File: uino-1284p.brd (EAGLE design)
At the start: 68.6 x 53.3 mm, 59 parts, among them J1 Micro USB, J2 M03X2, J3 CON_TERMINAL_BLOCK_02-5MM, J4 M03X2, J5 IO, U1 ATMEGA8U2AU, U2 LD117AS50TR, U3 ATMEGA1284AU, X1 16MHz, X2 16MHz

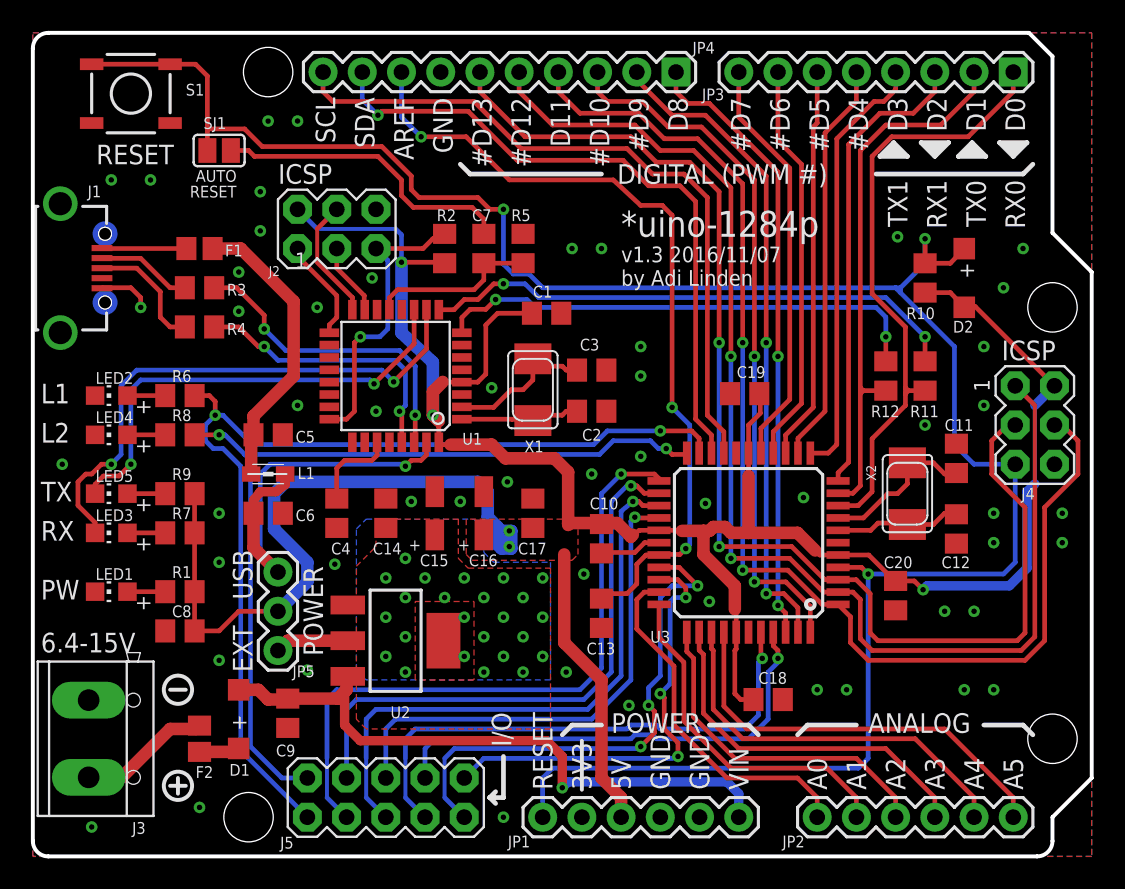
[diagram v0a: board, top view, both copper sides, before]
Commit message: Replaced reverse polarity schottky with P-FET.
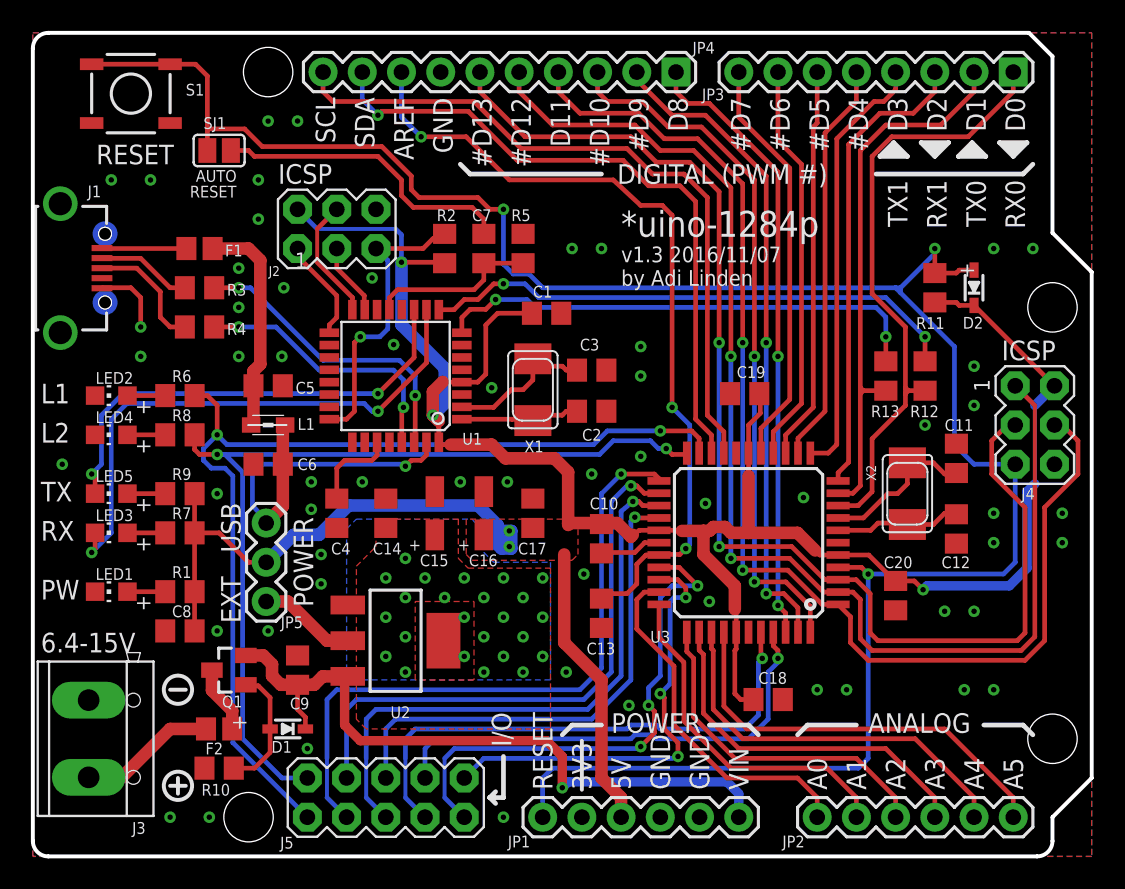
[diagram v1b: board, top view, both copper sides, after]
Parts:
- added Q1: (no value), transistor-fet:SOT23
- added R13: 1k, rcl:R0805
- D1: value 1A -> 6.2V; device diode:SOD123 -> diode:SOD323
- D2: device diode:SOD123 -> diode:SOD323
- R10: value 10k -> 1k
- R11: value 1k -> 10k
- moved R10 55.7 mm to (12.1, 5.71), turned to 0 degrees
- moved R11 5.75 mm to (58.4, 36.8), turned to 270 degrees
- moved JP5 3.27 mm to (15.1, 16.5)
- moved D1 3.24 mm to (16.5, 8.26), turned to 180 degrees
- moved C5 3.18 mm to (15.2, 30.5)
- moved L1 3.18 mm to (15.2, 27.9)
- moved C6 3.17 mm to (15.2, 25.4), turned to 180 degrees
- moved C9 2.87 mm to (17.1, 12.1), turned to 90 degrees
- moved R12 2.54 mm to (57.8, 31.1)
- moved F2 1.42 mm to (12.1, 8.26), turned to 0 degrees
- moved D2 0.90 mm to (61.0, 36.8)
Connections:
- new net N$18: D1.A, Q1.1, R10.2
- net D0: now also R12.1; no longer R11.1
- net D1: now also R13.1; no longer R12.1
- net GND: now also R10.1
- net N$1: now also Q1.3; no longer D1.A
- net N$6: now also R12.2; no longer R11.2
- net N$7: now also R13.2; no longer R12.2
- net RESET: now also R11.1; no longer R10.1
- net VCC: now also R11.2; no longer R10.2
- net VIN: now also Q1.2
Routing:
- net VCC: track 192.0 -> 182.1 mm
- net N$18: track 0.00 -> 8.24 mm
- net N$2: track 19.0 -> 14.3 mm
- net UVCC: track 27.5 -> 23.3 mm
- net VIN: track 41.0 -> 44.4 mm
- net N$1: track 2.63 -> 4.35 mm
- net EVCC: track 4.78 -> 6.34 mm
- net GND: track 7.43 -> 8.70 mm, vias 54 -> 58
- net D-: track 20.6 -> 19.7 mm
- net RESET: track 143.7 -> 143.0 mm
- net D+: track 18.4 -> 17.8 mm
- net N$29: track 35.7 -> 36.3 mm

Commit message: Fixed values and numbering.
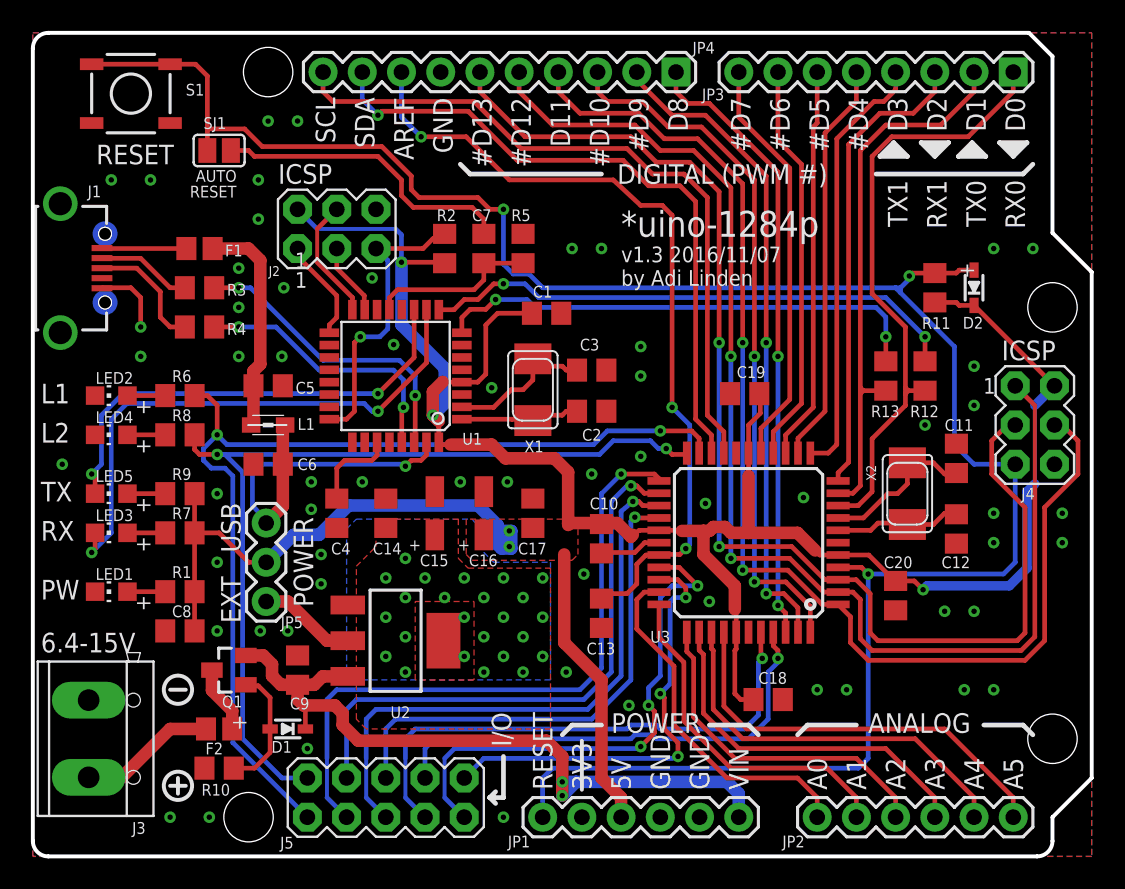
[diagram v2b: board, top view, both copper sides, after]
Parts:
- R10: value 1k -> 100k
- SJ1: value AUTO_RESET_EN -> (none)
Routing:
- net VIN: track 44.4 -> 47.5 mm, vias 1 -> 2
- net RESET: track 143.0 -> 140.7 mm
- net GND: vias 58 -> 60
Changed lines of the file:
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@@
 <text x="20.8578" y="49.1622" size="1.27" layer="21" font="vector" ratio="16" rot="R270">SDA</text>
 <text x="18.3178" y="49.1622" size="1.27" layer="21" font="vector" ratio="16" rot="R270">SCL</text>
-<text x="61.9716" y="30.1112" size="1.016" layer="21" font="vector" ratio="12" rot="R90">1</text>
+<text x="62.3448" y="30.9836" size="1.016" layer="21" font="vector" ratio="12" rot="R180">1</text>
 <text x="62.7502" y="32.1354" size="1.27" layer="21" font="vector" ratio="16">ICSP</text>
 <text x="15.8872" y="43.5654" size="1.27" layer="21" font="vector" ratio="16">ICSP</text>
@@
 <wire x1="9.398" y1="4.064" x2="9.398" y2="5.08" width="0.254" layer="21"/>
 <text x="25.1338" y="20.5696" size="0.762" layer="21" font="vector" ratio="18" rot="R180">+</text>
+<text x="17.7678" y="37.8416" size="1.016" layer="21" font="vector" ratio="12" rot="R180">1</text>
 </plain>
 <attributes>
@@
 </element>
 <element name="R11" library="rcl" package="R0805" value="10k" x="58.42" y="36.83" smashed="yes" rot="R270">
-<attribute name="NAME" x="59.055" y="34.925" size="0.762" layer="25" font="vector" ratio="18" rot="R180"/>
+<attribute name="NAME" x="59.436" y="34.925" size="0.762" layer="25" font="vector" ratio="18" rot="R180"/>
 <attribute name="VALUE" x="55.88" y="37.465" size="1.27" layer="27" rot="R270"/>
 </element>
@@
 <attribute name="VALUE" x="47.371" y="32.512" size="1.27" layer="27" rot="R180"/>
 </element>
-<element name="SJ1" library="jumper" package="SJ" value="AUTO_RESET_EN" x="12.065" y="45.72" smashed="yes" rot="R180">
+<element name="SJ1" library="jumper" package="SJ" value="" x="12.065" y="45.72" smashed="yes" rot="R180">
 <attribute name="NAME" x="11.049" y="47.117" size="0.762" layer="25" font="vector" ratio="18"/>
 <attribute name="VALUE" x="11.6649" y="45.72" size="0.02" layer="27" rot="R180"/>
@@
 <attribute name="VALUE" x="17.41" y="10.06" size="0.8128" layer="27" ratio="10" rot="R180"/>
 </element>
-<element name="R10" library="rcl" package="R0805" value="1k" x="12.065" y="5.715" smashed="yes">
+<element name="R10" library="rcl" package="R0805" value="100k" x="12.065" y="5.715" smashed="yes">
 <attribute name="NAME" x="10.922" y="3.937" size="0.762" layer="25" ratio="18"/>
 <attribute name="VALUE" x="11.43" y="3.175" size="1.27" layer="27"/>
@@
 <wire x1="63.627" y1="25.4" x2="60.96" y2="25.4" width="0.3048" layer="16"/>
 <wire x1="55.88" y1="36.83" x2="56.2" y2="36.83" width="0.3048" layer="16"/>
-<wire x1="58.42" y1="39.37" x2="58.42" y2="37.78" width="0.3048" layer="1"/>
-<wire x1="58.42" y1="37.78" x2="59.806" y2="37.78" width="0.3048" layer="1"/>
 <wire x1="56.2" y1="36.51" x2="56.2" y2="36.83" width="0.3048" layer="16"/>
 <wire x1="59.69" y1="33.02" x2="56.2" y2="36.51" width="0.3048" layer="16"/>
@@
 <via x="54.102" y="18.288" extent="1-16" drill="0.35"/>
 <via x="30.48" y="41.91" extent="1-16" drill="0.35"/>
-<via x="58.42" y="39.37" extent="1-16" drill="0.35"/>
+<via x="56.769" y="37.592" extent="1-16" drill="0.35"/>
 <wire x1="33.02" y1="36.83" x2="32.131" y2="37.719" width="0.3048" layer="16"/>
 <wire x1="32.131" y1="37.719" x2="31.115" y2="37.719" width="0.3048" layer="16"/>
@@
 <wire x1="59.806" y1="37.78" x2="59.999" y2="37.973" width="0.3048" layer="1"/>
 <wire x1="59.999" y1="37.973" x2="60.96" y2="37.973" width="0.3048" layer="1"/>
-<wire x1="56.2" y1="36.83" x2="58.42" y2="39.05" width="0.3048" layer="16"/>
-<wire x1="58.42" y1="39.05" x2="58.42" y2="39.37" width="0.3048" layer="16"/>
+<wire x1="58.42" y1="37.78" x2="56.957" y2="37.78" width="0.3048" layer="1"/>
+<wire x1="56.957" y1="37.78" x2="56.769" y2="37.592" width="0.3048" layer="1"/>
+<wire x1="59.806" y1="37.78" x2="58.42" y2="37.78" width="0.3048" layer="1"/>
+<wire x1="56.2" y1="36.83" x2="56.769" y2="37.399" width="0.3048" layer="16"/>
+<wire x1="56.769" y1="37.399" x2="56.769" y2="37.592" width="0.3048" layer="16"/>
 </signal>
 <signal name="3V3">
@@
 <contactref element="U2" pad="3"/>
 <contactref element="C9" pad="1"/>
-<wire x1="21.209" y1="7.493" x2="33.274" y2="7.493" width="0.6096" layer="1"/>
-<wire x1="45.72" y1="4.064" x2="45.72" y2="2.54" width="0.6096" layer="16"/>
-<wire x1="44.958" y1="4.826" x2="45.72" y2="4.064" width="0.6096" layer="16"/>
-<wire x1="34.671" y1="4.826" x2="44.958" y2="4.826" width="0.6096" layer="16"/>
-<wire x1="34.29" y1="4.445" x2="34.671" y2="4.826" width="0.6096" layer="16"/>
-<wire x1="34.29" y1="6.477" x2="34.29" y2="4.445" width="0.6096" layer="1"/>
-<wire x1="33.274" y1="7.493" x2="34.29" y2="6.477" width="0.6096" layer="1"/>
-<via x="34.29" y="4.445" extent="1-16" drill="0.35"/>
-<wire x1="20.32" y1="11.5824" x2="20.3962" y2="11.6586" width="0.8128" layer="1"/>
-<wire x1="21.209" y1="7.493" x2="20.193" y2="8.509" width="0.6096" layer="1"/>
-<wire x1="20.193" y1="8.509" x2="20.193" y2="11.303" width="0.6096" layer="1"/>
+<wire x1="21.082" y1="7.493" x2="33.274" y2="7.493" width="0.8128" layer="1"/>
+<wire x1="45.72" y1="4.064" x2="45.72" y2="2.54" width="0.8128" layer="16"/>
+<wire x1="44.958" y1="4.826" x2="45.72" y2="4.064" width="0.8128" layer="16"/>
+<wire x1="35.179" y1="4.826" x2="44.958" y2="4.826" width="0.8128" layer="16"/>
+<wire x1="33.274" y1="7.493" x2="34.29" y2="6.477" width="0.8128" layer="1"/>
+<via x="34.29" y="3.937" extent="1-16" drill="0.35"/>
 <contactref element="Q1" pad="2"/>
 <contactref element="D1" pad="C"/>
@@
 <wire x1="18.227" y1="11.115" x2="18.7706" y2="11.6586" width="0.8128" layer="1"/>
 <wire x1="20.3962" y1="11.6586" x2="18.7706" y2="11.6586" width="0.8128" layer="1"/>
-<wire x1="17.653" y1="8.255" x2="17.653" y2="9.017" width="0.3048" layer="1"/>
-<wire x1="17.653" y1="9.017" x2="17.145" y2="9.525" width="0.3048" layer="1"/>
-<wire x1="17.145" y1="9.525" x2="17.145" y2="11.115" width="0.3048" layer="1"/>
-<wire x1="20.32" y1="11.5824" x2="20.193" y2="11.303" width="0" layer="19" extent="1-1"/>
+<via x="34.29" y="4.826" extent="1-16" drill="0.35"/>
+<wire x1="35.179" y1="4.826" x2="34.29" y2="3.937" width="0.8128" layer="16"/>
+<wire x1="34.29" y1="4.826" x2="35.179" y2="4.826" width="0.8128" layer="16"/>
+<wire x1="34.29" y1="4.826" x2="34.29" y2="4.064" width="0.8128" layer="16"/>
+<wire x1="34.29" y1="6.477" x2="34.29" y2="3.937" width="0.8128" layer="1"/>
+<wire x1="17.145" y1="11.115" x2="17.145" y2="10.16" width="0.8128" layer="1"/>
+<wire x1="17.145" y1="10.16" x2="17.526" y2="9.779" width="0.8128" layer="1"/>
+<wire x1="21.082" y1="7.493" x2="20.066" y2="8.509" width="0.8128" layer="1"/>
+<wire x1="20.066" y1="8.509" x2="20.066" y2="9.271" width="0.8128" layer="1"/>
+<wire x1="20.066" y1="9.271" x2="19.558" y2="9.779" width="0.8128" layer="1"/>
+<wire x1="19.558" y1="9.779" x2="17.526" y2="9.779" width="0.8128" layer="1"/>
+<wire x1="17.653" y1="8.255" x2="17.653" y2="9.652" width="0.3048" layer="1"/>
+<wire x1="17.653" y1="9.652" x2="17.526" y2="9.779" width="0.3048" layer="1"/>
 </signal>
 <signal name="GND" airwireshidden="yes">
@@
 <via x="34.925" y="39.37" extent="1-16" drill="0.35"/>
 <via x="39.37" y="31.115" extent="1-16" drill="0.35"/>
-<via x="15.24" y="14.605" extent="1-16" drill="0.35"/>
+<via x="14.732" y="14.605" extent="1-16" drill="0.35"/>
 <via x="15.24" y="47.625" extent="1-16" drill="0.35"/>
 <via x="17.145" y="47.625" extent="1-16" drill="0.35"/>
@@
 <via x="11.43" y="2.54" extent="1-16" drill="0.35"/>
 <via x="18.669" y="19.558" extent="1-16" drill="0.35"/>
+<via x="11.938" y="19.05" extent="1-16" drill="0.35"/>
+<via x="16.51" y="14.605" extent="1-16" drill="0.35"/>
 </signal>
 <signal name="A0">

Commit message: Changed tantalum to 0805 and ceramic.  Made use of extra space.
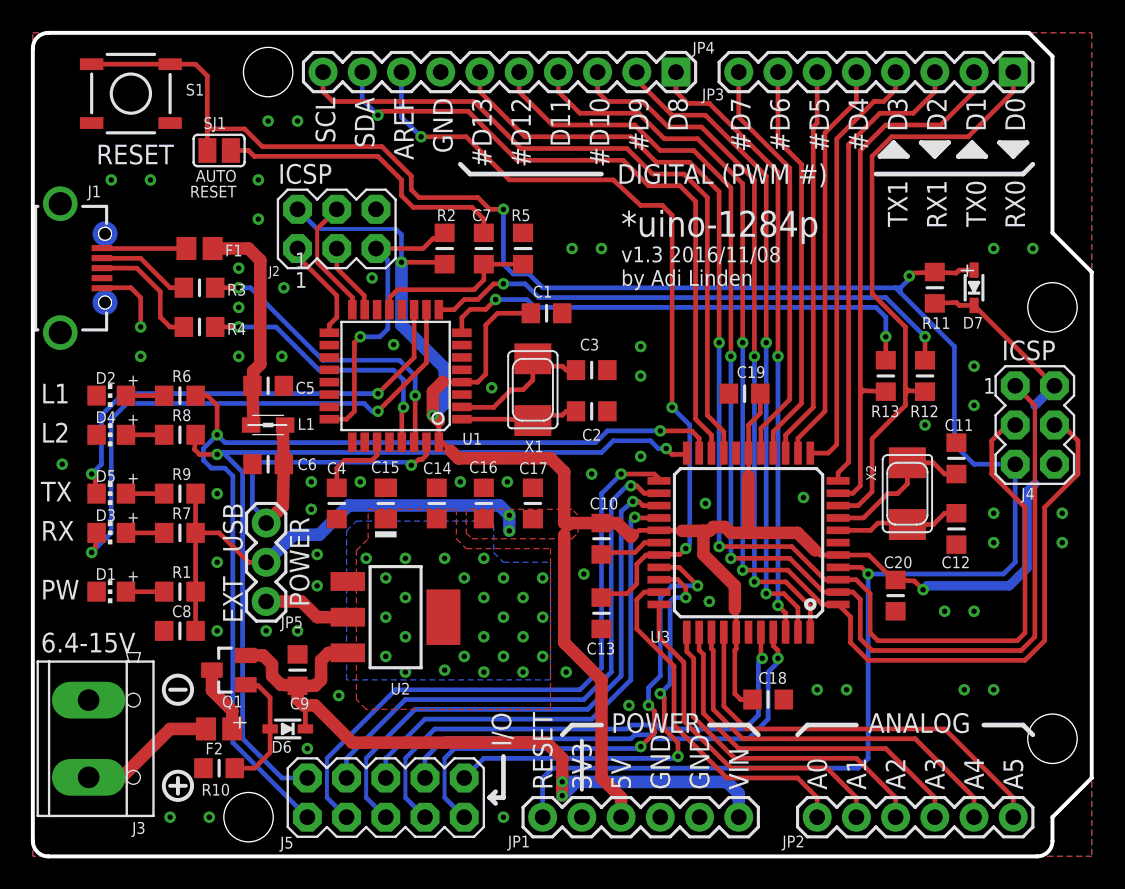
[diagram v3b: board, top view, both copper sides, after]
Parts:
- removed LED1: PWR (Green), adafruit:CHIP-LED0805
- removed LED2: L1 (Red), adafruit:CHIP-LED0805
- removed LED3: RX (Yellow), adafruit:CHIP-LED0805
- removed LED4: L2 (Red), adafruit:CHIP-LED0805
- removed LED5: TX (Yellow), adafruit:CHIP-LED0805
- added D3: RX (Yellow), led:CHIP-LED0805MP
- added D4: L2 (Red), led:CHIP-LED0805MP
- added D5: TX (Yellow), led:CHIP-LED0805MP
- added D6: 6.2V, diode:SOD323
- added D7: (no value), diode:SOD323
- C1, C10, C11, C12, C13, C14, C17, C18, C19, C2, C20, C3, C4, C5, C6, C7, C8: device rcl:C0805 -> rc-master-smd:C0805MP
- C15: device rcl:CT3216 -> rc-master-smd:C0805MP/T
- C16: device rcl:CT3216 -> rc-master-smd:C0805MP
- C9: value 0.1u -> 10u; device rcl:C0805 -> rc-master-smd:C0805MP
- D1: value 6.2V -> PWR (Green); device diode:SOD323 -> led:CHIP-LED0805MP
- D2: value 500mA -> L1 (Red); device diode:SOD323 -> led:CHIP-LED0805MP
- R1, R10, R11, R12, R13, R2, R3, R4, R5, R6, R7, R8, R9: device rcl:R0805 -> rc-master-smd:R0805MP
- moved D2 56.3 mm to (5.08, 29.8)
- moved D1 14.5 mm to (5.08, 17.1), turned to 90 degrees
- moved C14 3.36 mm to (26.2, 22.9)
- moved C15 3.24 mm to (22.9, 22.9), turned to 270 degrees
- moved U2 1.52 mm to (23.5, 15.5)
- moved C16 0.63 mm to (29.2, 22.9)
- moved C17 0.63 mm to (32.4, 22.9)
- moved C4 0.63 mm to (19.7, 22.9)
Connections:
- net GND: now also C16.2, D1.C, D2.C, D4.C; no longer C16.-, LED1.C, LED2.C, LED4.C
- net N$11: now also D2.A; no longer LED2.A
- net N$12: now also D4.A; no longer LED4.A
- net N$18: now also D6.A; no longer D1.A
- net N$26: now also D3.A; no longer LED3.A
- net N$27: now also D5.A; no longer LED5.A
- net N$29: now also D3.C; no longer LED3.C
- net N$30: now also D5.C; no longer LED5.C
- net N$34: now also D1.A; no longer LED1.A
- net RESET: now also D7.A; no longer D2.A
- net VCC: now also C16.1, D7.C; no longer C16.+, D2.C
- net VIN: now also D6.C; no longer D1.C
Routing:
- net D18: track 42.6 -> 40.4 mm
- net VCC: track 182.1 -> 180.0 mm
- net D19: track 37.3 -> 35.5 mm
- net D20: track 38.0 -> 36.5 mm
- net D21: track 32.6 -> 31.5 mm
- net VIN: track 47.5 -> 48.3 mm
- net D22: track 34.8 -> 34.1 mm
- net N$10: track 5.77 -> 5.07 mm
- net EVCC: track 6.34 -> 5.70 mm, vias 24 -> 25
- net GND: track 8.70 -> 8.76 mm, vias 60 -> 61
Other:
- board text added: "v1.3 2016/11/08"
- board text removed: "v1.3 2016/11/07"
